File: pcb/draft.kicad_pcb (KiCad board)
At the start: 2 copper layers, 54 x 54 mm, 36 parts, among them J1 1-MALE, J10 TC2030_NL, J11 1-MALE, J12 1-FEMALE, J13 2-MALE, J14 2-FEMALE, J15 3-MALE, J16 3-FEMALE, J17 4-MALE, J18 4-FEMALE, J2 1-FEMALE, J3 2-MALE, J4 2-FEMALE, J5 3-MALE, J6 3-FEMALE, J7 4-MALE, J8 4-FEMALE, U3 ATmega328P-MU

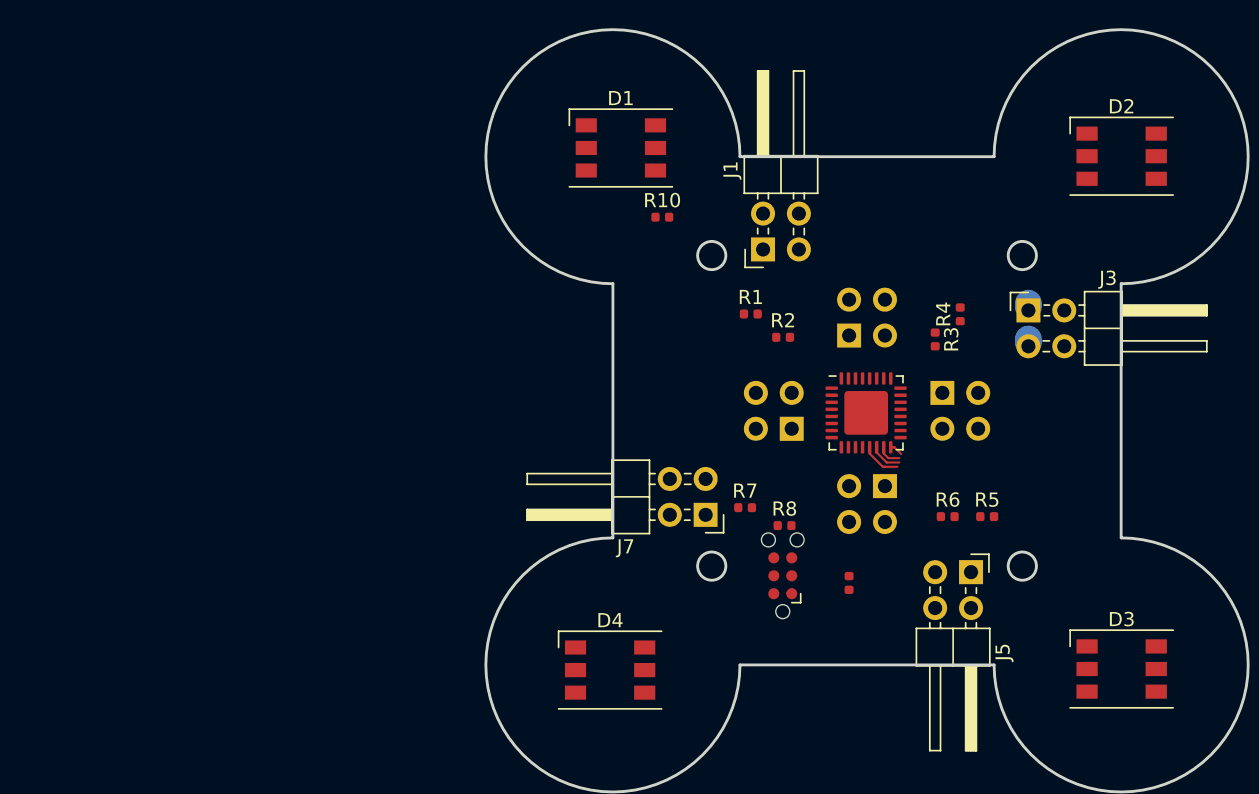
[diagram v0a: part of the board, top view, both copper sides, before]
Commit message: Place footprints
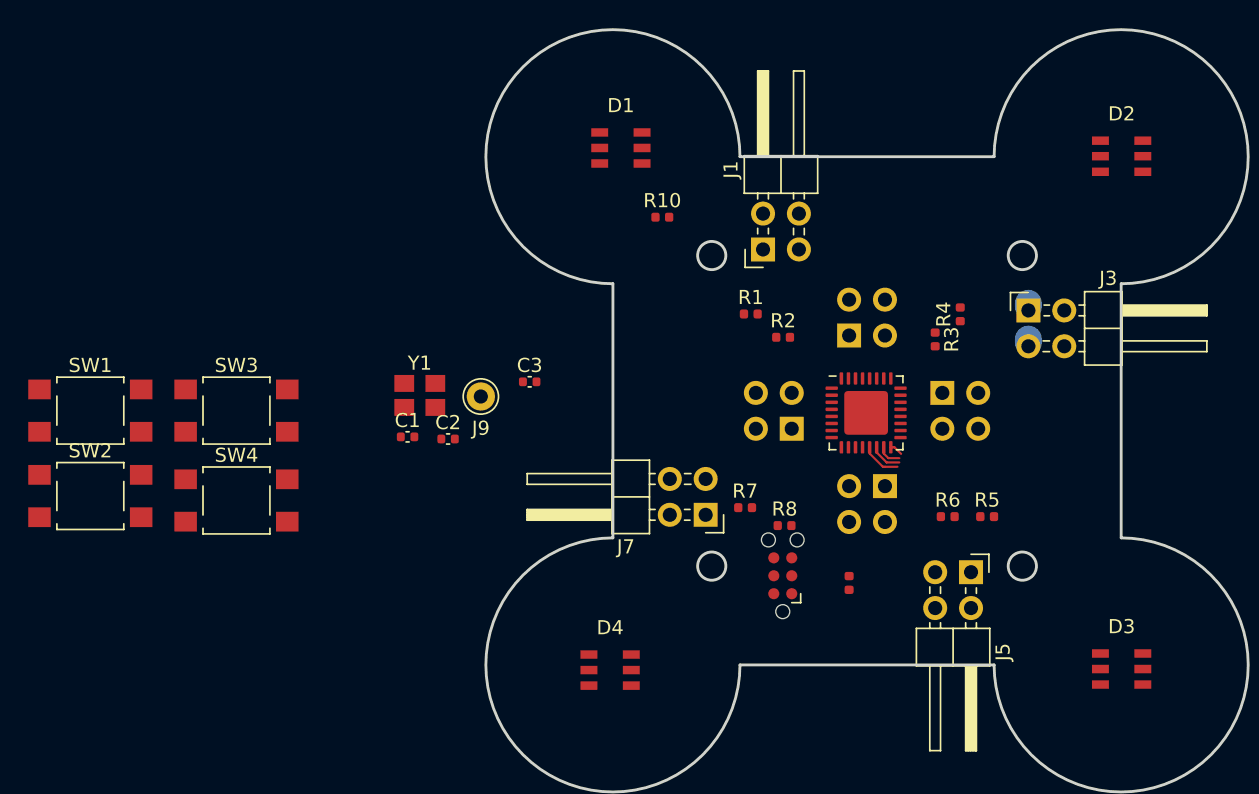
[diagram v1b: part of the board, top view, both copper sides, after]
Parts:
- added C1: 0.1u, Capacitor_SMD:C_0402_1005Metric, F.Cu at (109.4, 78.3)
- added C2: 12p, Capacitor_SMD:C_0402_1005Metric, F.Cu at (112.3, 78.4)
- added C3: 12p, Capacitor_SMD:C_0402_1005Metric, F.Cu at (118.1, 74.4)
- added J9: DTR, Connector_Pin:Pin_D1.0mm_L10.0mm, F.Cu at (114.6, 75.4)
- added SW1: ACTION, Button_Switch_SMD:SW_SPST_TL3305A, F.Cu at (87.0, 76.4)
- added SW2: ACTION, Button_Switch_SMD:SW_SPST_TL3305A, F.Cu at (87.0, 82.5)
- added SW3: ACTION, Button_Switch_SMD:SW_SPST_TL3305A, F.Cu at (97.3, 76.4)
- added SW4: ACTION, Button_Switch_SMD:SW_SPST_TL3305A, F.Cu at (97.3, 82.8)
- added Y1: YSX321SL, node:YSX321SL, F.Cu at (110.3, 75.4)
- D1, D2, D3, D4: footprint LED_SMD:LED_WS2812_PLCC6_5.0x5.0mm_P1.6mm -> node:WS2813-Mini
- J1, J11: value 1-MALE -> MALE
- J12, J2: value 1-FEMALE -> FEMALE
- J13, J3: value 2-MALE -> MALE
- J14, J4: value 2-FEMALE -> FEMALE
- J15, J5: value 3-MALE -> MALE
- J16, J6: value 3-FEMALE -> FEMALE
- J17, J7: value 4-MALE -> MALE
- J18, J8: value 4-FEMALE -> FEMALE

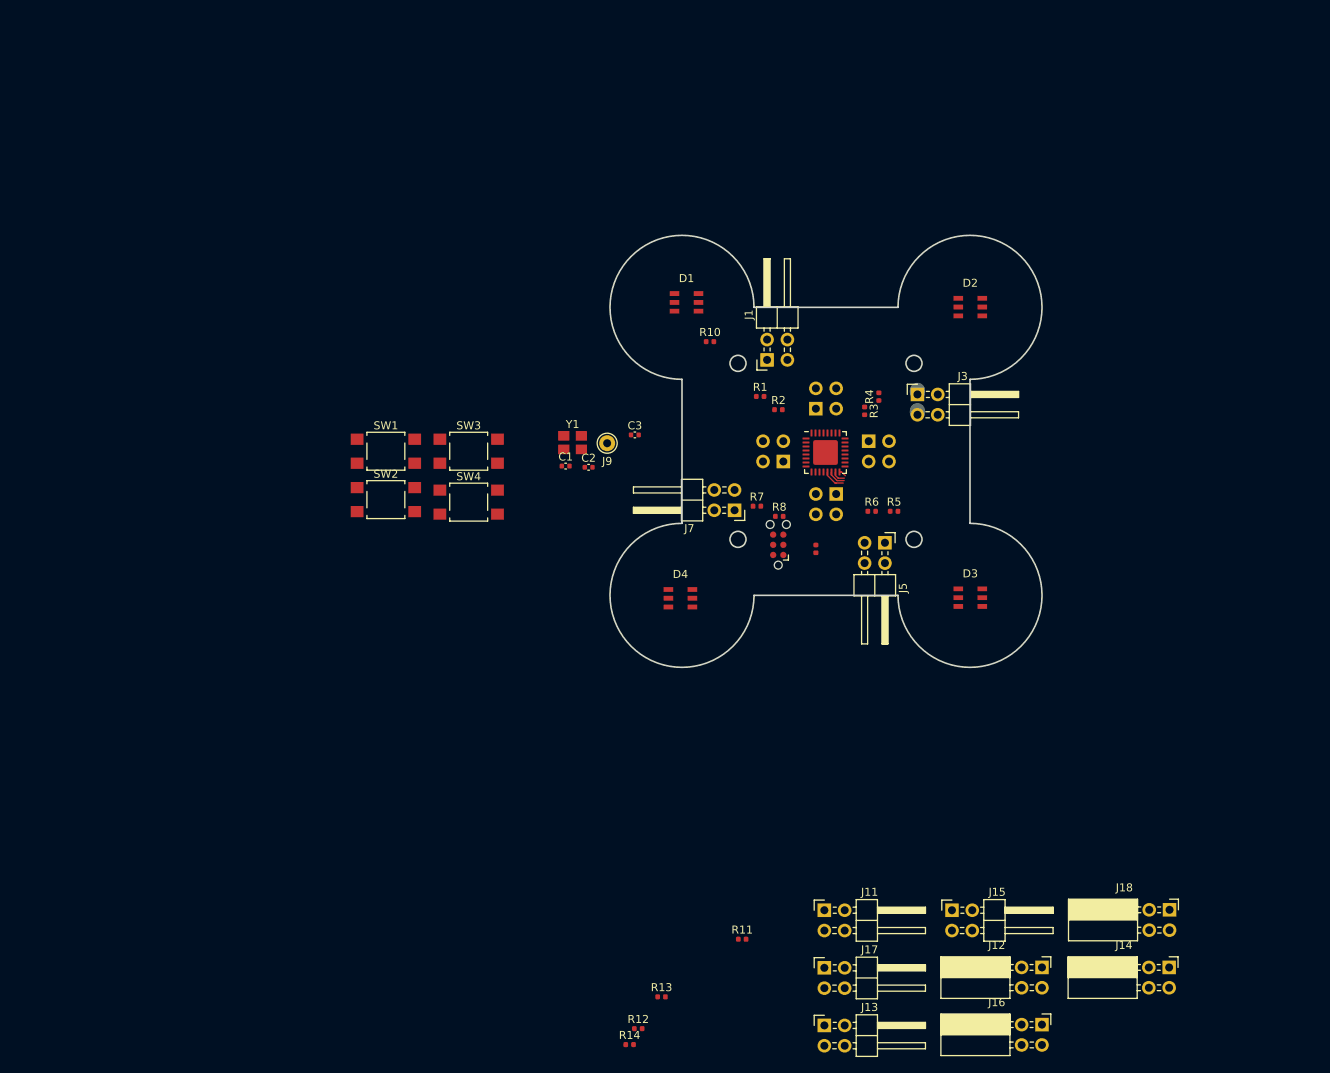
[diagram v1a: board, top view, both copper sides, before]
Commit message: Add buzzer and clean up
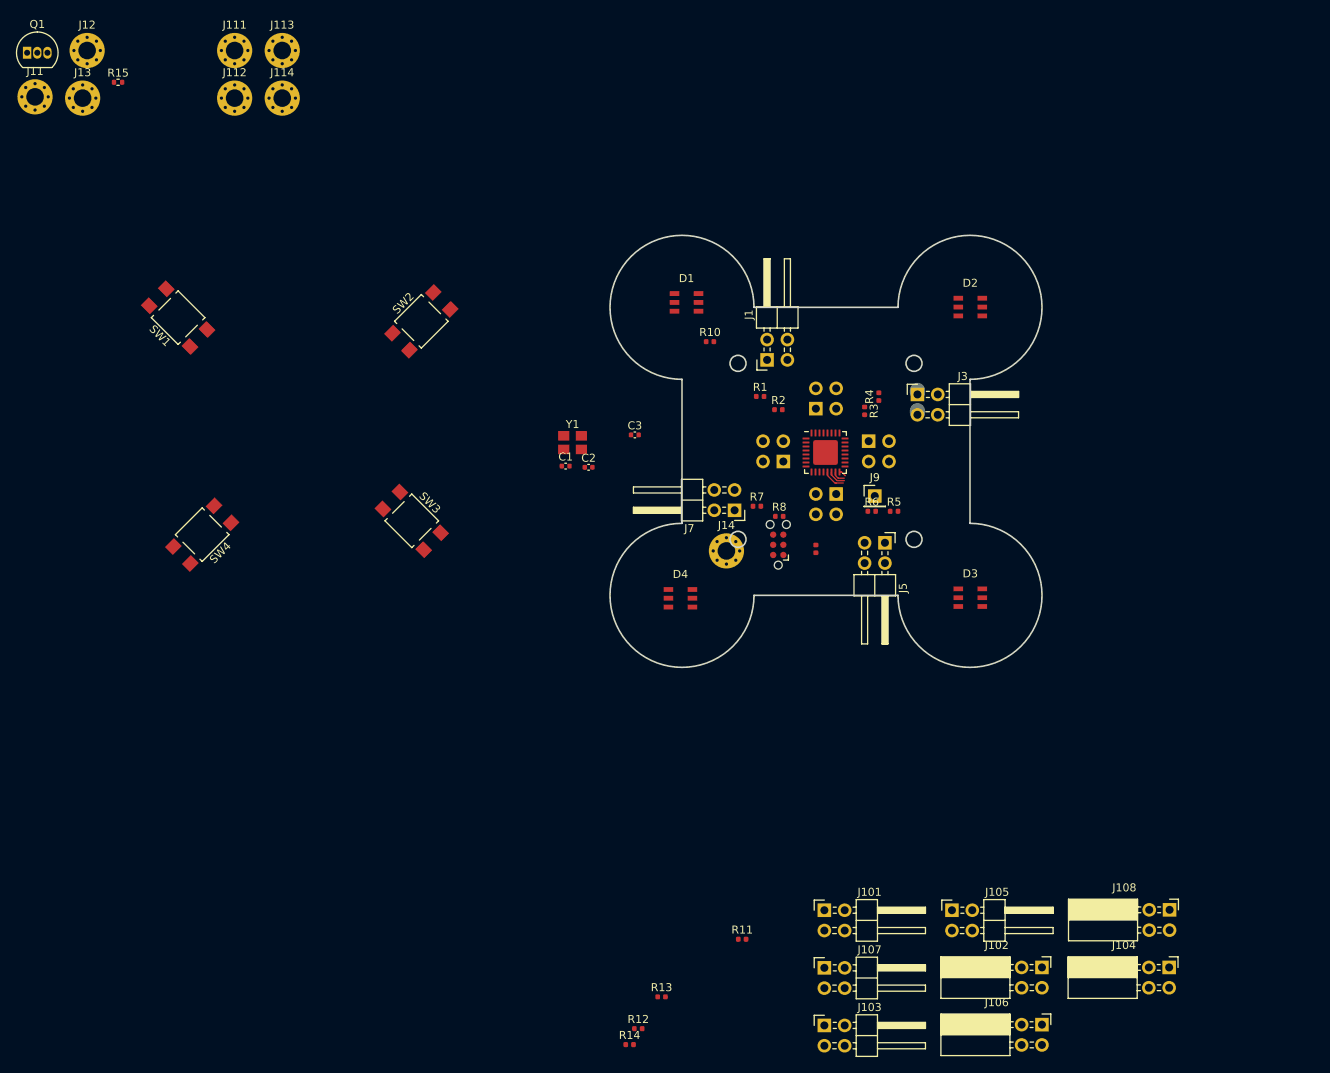
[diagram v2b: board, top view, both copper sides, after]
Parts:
- added J11: STANDOFF, MountingHole:MountingHole_2.2mm_M2_Pad_Via, F.Cu at (43.1, 32.1)
- added J111: STANDOFF, MountingHole:MountingHole_2.2mm_M2_Pad_Via, F.Cu at (68.1, 26.4)
- added J112: STANDOFF, MountingHole:MountingHole_2.2mm_M2_Pad_Via, F.Cu at (68.1, 32.3)
- added J113: STANDOFF, MountingHole:MountingHole_2.2mm_M2_Pad_Via, F.Cu at (74.0, 26.4)
- added J114: STANDOFF, MountingHole:MountingHole_2.2mm_M2_Pad_Via, F.Cu at (74.0, 32.3)
- added J12: STANDOFF, MountingHole:MountingHole_2.2mm_M2_Pad_Via, F.Cu at (49.6, 26.4)
- added J13: STANDOFF, MountingHole:MountingHole_2.2mm_M2_Pad_Via, F.Cu at (49.1, 32.3)
- added J14: STANDOFF, MountingHole:MountingHole_2.2mm_M2_Pad_Via, F.Cu at (129.5, 88.9)
- added Q1: PN2222A, Package_TO_SOT_THT:TO-92_Inline, F.Cu at (42.1, 26.6)
- added R15: 470, Resistor_SMD:R_0402_1005Metric, F.Cu at (53.5, 30.3)
- J9: footprint Connector_Pin:Pin_D1.0mm_L10.0mm -> Connector_PinHeader_2.54mm:PinHeader_1x01_P2.54mm_Vertical
- moved J9 34.1 mm to (148.1, 82.0)
- moved SW4 33.6 mm to (64.0, 86.9), turned to 225 degrees
- moved SW1 30.9 mm to (61.0, 59.7), turned to 135 degrees
- moved SW2 22.7 mm to (91.4, 60.2), turned to 45 degrees
- moved SW3 11.2 mm to (90.2, 85.1), turned to 315 degrees
- renumbered J11 to J101, J12 to J102, J13 to J103, J14 to J104, J15 to J105, J16 to J106, J17 to J107, J18 to J108
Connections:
- net +5V renamed +5VB
- D1 pad 5: GND -> GNDB
- D1 pad 6: GND -> GNDB
- D2 pad 5: GND -> GNDB
- D3 pad 5: GND -> GNDB
- D4 pad 5: GND -> GNDB
- J1 pad 3: GND -> GNDB
- J10 pad 1: GND -> GNDB
- J2 pad 3: GND -> GNDB
- J3 pad 3: GND -> GNDB
- J4 pad 3: GND -> GNDB
- J5 pad 3: GND -> GNDB
- J6 pad 3: GND -> GNDB
- J7 pad 3: GND -> GNDB
- J8 pad 3: GND -> GNDB
- R12 pad 1: /Bottom/BUTTON2 -> Net-(J12-Pad1)
- R13 pad 1: /Bottom/BUTTON3 -> Net-(J13-Pad1)
- R14 pad 1: /Bottom/BUTTON4 -> Net-(J14-Pad1)
- SW1 pad 1: /Top/BUTTON1 -> Net-(J111-Pad1)
- SW2 pad 1: /Top/BUTTON2 -> Net-(J112-Pad1)
- SW3 pad 1: /Top/BUTTON3 -> Net-(J113-Pad1)
- SW4 pad 1: /Top/BUTTON4 -> Net-(J114-Pad1)
- U3 pad 21: GND -> GNDB
- U3 pad 3: GND -> GNDB
- U3 pad 33: GND -> GNDB
- U3 pad 5: GND -> GNDB
- Y1 pad 2: GND -> GNDB
- Y1 pad 4: GND -> GNDB

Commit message: Precisely position some components
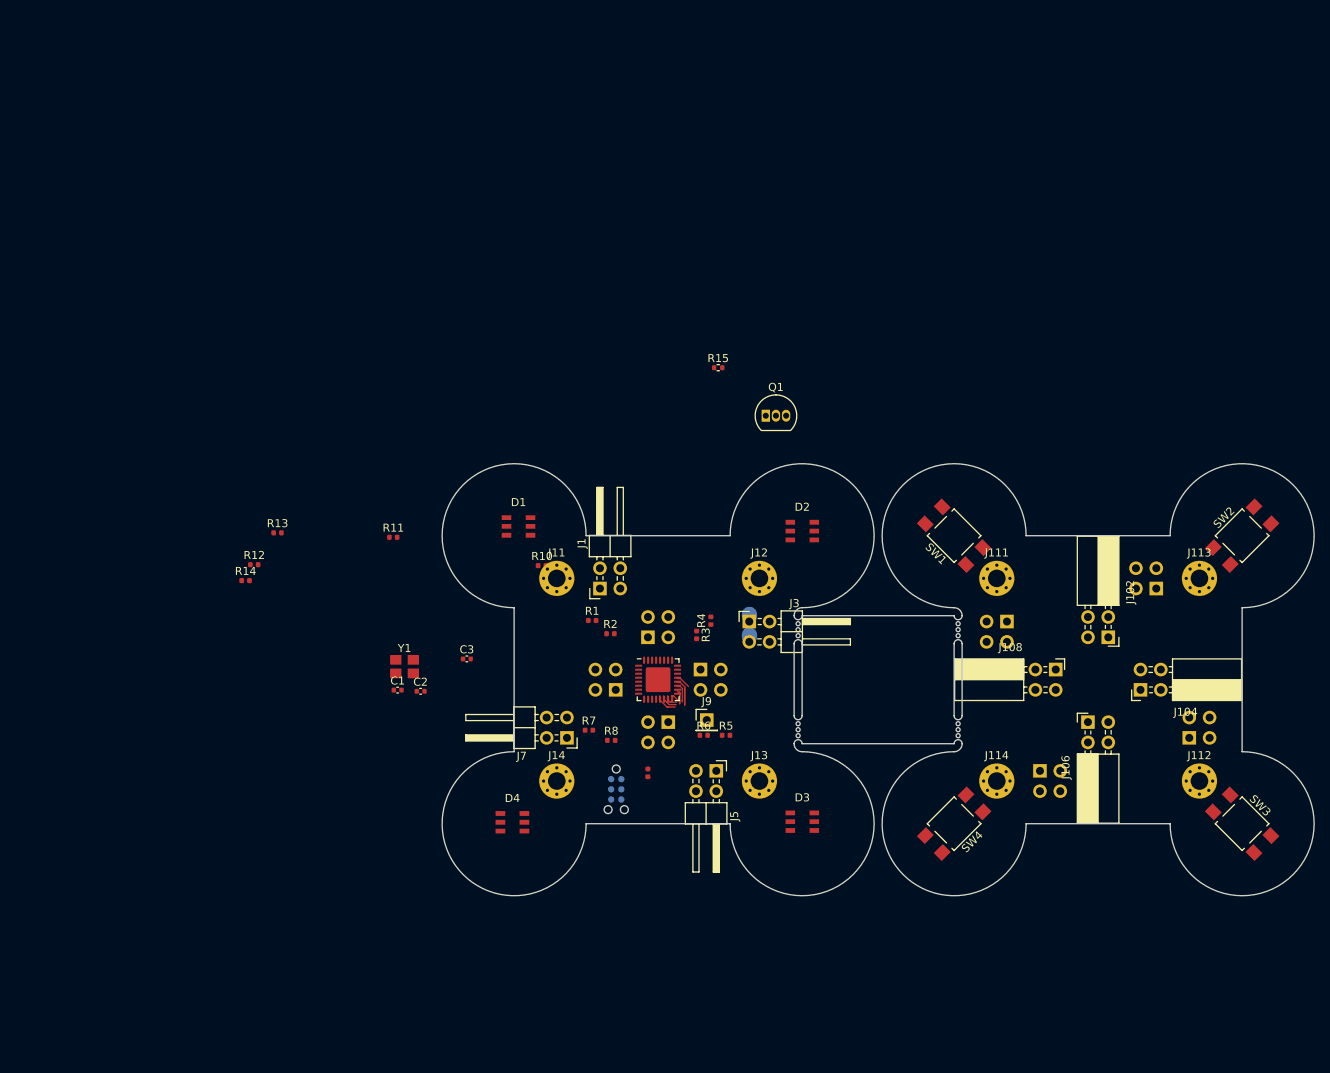
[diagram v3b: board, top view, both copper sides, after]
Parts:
- added mouse-bite: VAL**, node:mouse-bite, F.Cu at (138.5, 98.8)
- added mouse-bite: VAL**, node:mouse-bite, F.Cu at (138.5, 111.2)
- added mouse-bite: VAL**, node:mouse-bite, F.Cu at (158.5, 111.2)
- added mouse-bite: VAL**, node:mouse-bite, F.Cu at (158.5, 98.8)
- J10, J101, J103, J105, J107: moved to B.Cu
- moved J112 147.8 mm to (188.7, 117.7)
- moved J113 132.3 mm to (188.7, 92.3)
- moved J114 123.6 mm to (163.3, 117.7)
- moved J13 120.2 mm to (133.7, 117.7)
- moved J111 115.9 mm to (163.3, 92.3)
- moved SW3 110.5 mm to (194.0, 123.0)
- moved J12 106.8 mm to (133.7, 92.3)
- moved SW2 106.0 mm to (194.0, 87.0)
- moved Q1 102.9 mm to (134.5, 72.0)
- moved SW1 100.8 mm to (158.0, 87.0)
- moved SW4 100.7 mm to (158.0, 123.0)
- moved J11 88.8 mm to (108.3, 92.3)
- moved R15 83.1 mm to (128.5, 66.0)
- moved R13 75.3 mm to (73.4, 86.6)
- moved R12 75.3 mm to (70.5, 90.6)
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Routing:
- net Net-(U3-Pad20): track 0.00 -> 5.70 mm
- net /Bottom/SCK: track 0.00 -> 3.29 mm
- net Net-(U3-Pad19): track 0.00 -> 2.48 mm
- net GNDB: track 0.25 -> 2.11 mm
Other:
- board size 54 x 54 mm -> 109 x 54 mm

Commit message: Select transistor for buzzer
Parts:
- added R16: 47, Resistor_SMD:R_0402_1005Metric, F.Cu at (179.0, 95.7)
- Q1: value PN2222A -> 2N3904; footprint Package_TO_SOT_THT:TO-92_Inline -> digikey-footprints:SOT23-6L
- SW1, SW2, SW3, SW4: footprint Button_Switch_SMD:SW_SPST_TL3305A -> node:TS-1187A-B-A-B
- moved D1 1.29 mm to (103.0, 87.0), turned to 45 degrees
- moved D2 0.58 mm to (139.0, 87.0), turned to 315 degrees
- moved D4 0.28 mm to (103.0, 123.0), turned to 135 degrees
- moved D3 0.26 mm to (139.0, 123.0), turned to 225 degrees
- turned SW1 to 45 degrees
- turned SW2 to 315 degrees
- turned SW3 to 225 degrees
- turned SW4 to 135 degrees
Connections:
- net /Bottom/BUTTON1 renamed Net-(J11-Pad1)
- C1 pad 2: Net-(C1-Pad2) -> /Bottom/~RST
- R9 pad 2: Net-(C1-Pad2) -> /Bottom/~RST
- U3 pad 29: Net-(C1-Pad2) -> /Bottom/~RST

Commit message: Fix: Wrong footprint for transistor
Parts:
- Q1: footprint digikey-footprints:SOT23-6L -> Package_TO_SOT_SMD:SOT-23
- moved Q1 4.24 mm to (130.6, 73.7)
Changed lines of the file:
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@@
       (net 68 "Net-(J114-Pad1)"))
   )
-  (module digikey-footprints:SOT23-6L (layer F.Cu)
-    (at 134.46 72)
-    (descr http://www.st.com/content/ccc/resource/technical/document/datasheet/9a/e6/1c/4f/b6/9a/44/e6/CD00047494.pdf/files/CD00047494.pdf/jcr:content/translations/en.CD00047494.pdf)
+  (module Package_TO_SOT_SMD:SOT-23 (layer F.Cu)
+    (at 130.556 73.66)
+    (descr "SOT-23, Standard")
+    (tags SOT-23)
     (attr smd)
-    (fp_text reference Q1 (at -0.025 -3.425) (layer F.SilkS)
+    (fp_text reference Q1 (at 0 -2.5) (layer F.SilkS)
       (effects (font (size 1 1) (thickness 0.15)))
     )
-    (fp_text value 2N3904 (at -0.05 3.6) (layer F.Fab)
+    (fp_text value 2N3904 (at 0 2.5) (layer F.Fab)
       (effects (font (size 1 1) (thickness 0.15)))
     )
-    (fp_line (start -1.525 -0.875) (end 1.525 -0.875) (layer F.Fab) (width 0.1))
-    (fp_line (start 1.525 -0.875) (end 1.525 0.875) (layer F.Fab) (width 0.1))
-    (fp_line (start 1.825 -2) (end 1.825 2) (layer F.CrtYd) (width 0.05))
-    (fp_line (start 1.825 -2) (end -1.825 -2) (layer F.CrtYd) (width 0.05))
-    (fp_line (start -1.825 -2) (end -1.825 2) (layer F.CrtYd) (width 0.05))
-    (fp_line (start -1.825 2) (end 1.825 2) (layer F.CrtYd) (width 0.05))
-    (fp_line (start -1.525 0.45) (end -1.1 0.875) (layer F.Fab) (width 0.1))
-    (fp_line (start -1.525 0.45) (end -1.525 -0.875) (layer F.Fab) (width 0.1))
-    (fp_line (start -1.1 0.875) (end 1.525 0.875) (layer F.Fab) (width 0.1))
-    (fp_line (start 1.65 -1) (end 1.65 -0.7) (layer F.SilkS) (width 0.1))
-    (fp_line (start 1.3 -1) (end 1.65 -1) (layer F.SilkS) (width 0.1))
-    (fp_line (start 1.65 1) (end 1.35 1) (layer F.SilkS) (width 0.1))
-    (fp_line (start 1.65 0.675) (end 1.65 1) (layer F.SilkS) (width 0.1))
-    (fp_line (start -1.65 -1) (end -1.65 -0.65) (layer F.SilkS) (width 0.1))
-    (fp_line (start -1.3 -1) (end -1.65 -1) (layer F.SilkS) (width 0.1))
-    (fp_line (start -1.325 0.825) (end -1.325 1.525) (layer F.SilkS) (width 0.1))
-    (fp_line (start -1.65 0.5) (end -1.325 0.825) (layer F.SilkS) (width 0.1))
-    (fp_text user %R (at 0 -0.05) (layer F.Fab)
-      (effects (font (size 0.75 0.75) (thickness 0.075)))
+    (fp_line (start 0.76 1.58) (end -0.7 1.58) (layer F.SilkS) (width 0.12))
+    (fp_line (start 0.76 -1.58) (end -1.4 -1.58) (layer F.SilkS) (width 0.12))
+    (fp_line (start -1.7 1.75) (end -1.7 -1.75) (layer F.CrtYd) (width 0.05))
+    (fp_line (start 1.7 1.75) (end -1.7 1.75) (layer F.CrtYd) (width 0.05))
+    (fp_line (start 1.7 -1.75) (end 1.7 1.75) (layer F.CrtYd) (width 0.05))
+    (fp_line (start -1.7 -1.75) (end 1.7 -1.75) (layer F.CrtYd) (width 0.05))
+    (fp_line (start 0.76 -1.58) (end 0.76 -0.65) (layer F.SilkS) (width 0.12))
+    (fp_line (start 0.76 1.58) (end 0.76 0.65) (layer F.SilkS) (width 0.12))
+    (fp_line (start -0.7 1.52) (end 0.7 1.52) (layer F.Fab) (width 0.1))
+    (fp_line (start 0.7 -1.52) (end 0.7 1.52) (layer F.Fab) (width 0.1))
+    (fp_line (start -0.7 -0.95) (end -0.15 -1.52) (layer F.Fab) (width 0.1))
+    (fp_line (start -0.15 -1.52) (end 0.7 -1.52) (layer F.Fab) (width 0.1))
+    (fp_line (start -0.7 -0.95) (end -0.7 1.5) (layer F.Fab) (width 0.1))
+    (fp_text user %R (at 0 0 90) (layer F.Fab)
+      (effects (font (size 0.5 0.5) (thickness 0.075)))
     )
-    (pad 1 smd rect (at -0.95 1.15) (size 0.6 1.2) (layers F.Cu F.Paste F.Mask)
+    (pad 1 smd rect (at -1 -0.95) (size 0.9 0.8) (layers F.Cu F.Paste F.Mask)
       (net 50 GNDB))
-    (pad 2 smd rect (at 0 1.15) (size 0.6 1.2) (layers F.Cu F.Paste F.Mask)
+    (pad 2 smd rect (at -1 0.95) (size 0.9 0.8) (layers F.Cu F.Paste F.Mask)
       (net 69 "Net-(Q1-Pad2)"))
-    (pad 3 smd rect (at 0.95 1.15) (size 0.6 1.2) (layers F.Cu F.Paste F.Mask)
+    (pad 3 smd rect (at 1 0) (size 0.9 0.8) (layers F.Cu F.Paste F.Mask)
       (net 70 "Net-(BZ1-Pad2)"))
-    (pad 4 smd rect (at 0.95 -1.15) (size 0.6 1.2) (layers F.Cu F.Paste F.Mask))
-    (pad 5 smd rect (at 0 -1.15) (size 0.6 1.2) (layers F.Cu F.Paste F.Mask))
-    (pad 6 smd rect (at -0.95 -1.15) (size 0.6 1.2) (layers F.Cu F.Paste F.Mask))
+    (model ${KISYS3DMOD}/Package_TO_SOT_SMD.3dshapes/SOT-23.wrl
+      (at (xyz 0 0 0))
+      (scale (xyz 1 1 1))
+      (rotate (xyz 0 0 0))
+    )
   )
   (gr_line (start 158 113) (end 139 113) (layer Edge.Cuts) (width 0.05))
